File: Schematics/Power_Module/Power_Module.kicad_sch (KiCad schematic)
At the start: 50 parts, among them J1 ScrewSwitch A, J2 ScrewSwitch B, J3 Battery B, J5 Battery A, J6 Stack Male Edge Connector, Q1 AO4447A, Q2 AO4447A, U1 LMR51430XDDCR, U2 LMR51430XDDCR, U3 LMR51430XDDCR

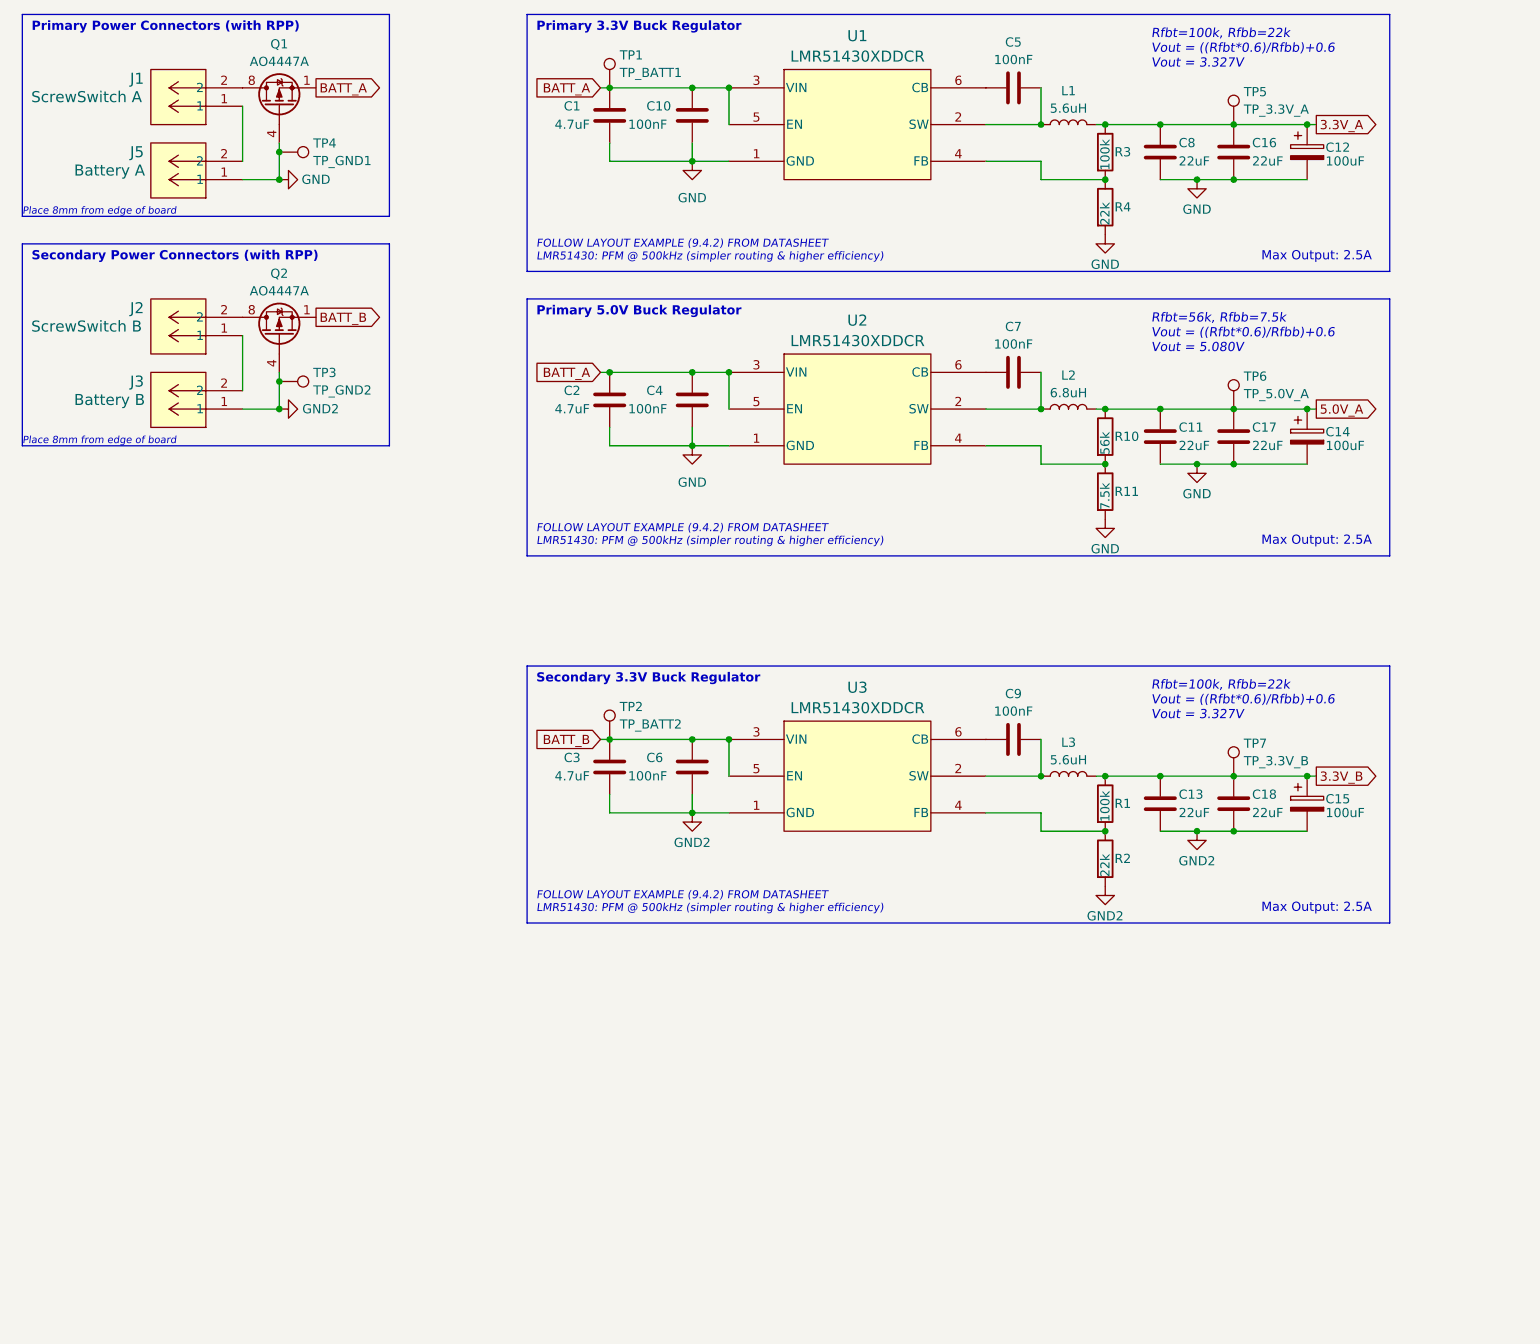
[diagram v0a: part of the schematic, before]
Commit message: Revision bump to V2.0
Changed to V2.0 due to significant hardware changes
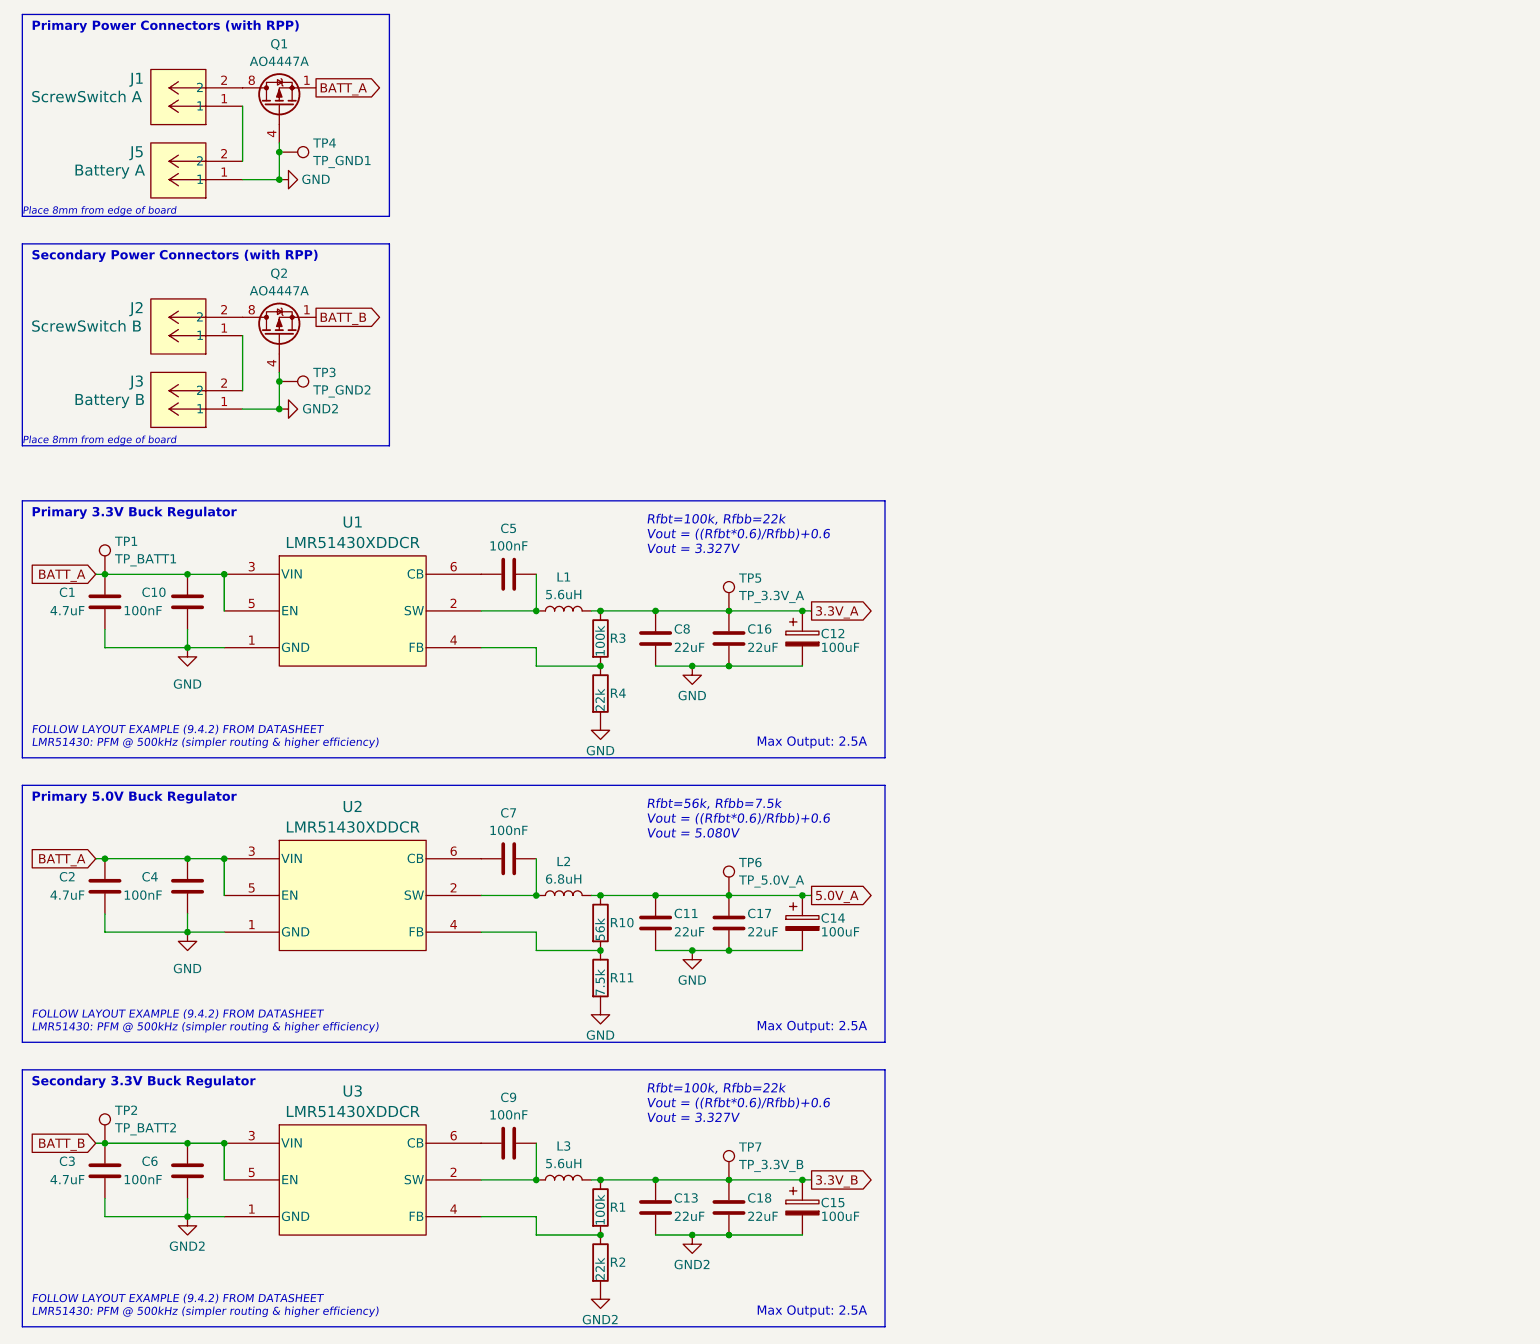
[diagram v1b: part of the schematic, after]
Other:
- title: QRET 23-24 SRAD Power Module -> QRET 23-25 SRAD Power Module
- moved on the sheet: C1, C10, C11, C12, C13, C14, C15, C16, C17, C18, C2, C3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

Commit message: Added MCUs + sensors to schematic
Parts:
- added C19, C20: 10uF, Capacitor_SMD:C_0603_1608Metric, symbol Device:C
- added C21, C22, C44, C45, C46: 0.1u, Capacitor_SMD:C_0603_1608Metric, symbol Device:C
- added C23, C24: 10p, Capacitor_SMD:C_0603_1608Metric, symbol Device:C
- added C25, C26, C27, C28, C29, C30, C31, C32: 100n, Capacitor_SMD:C_0402_1005Metric, symbol Device:C
- added C33, C36: 10n, Capacitor_SMD:C_0603_1608Metric, symbol Device:C
- added C34, C35, C37, C38: 1uF, Capacitor_SMD:C_0805_2012Metric, symbol Device:C_Polarized
- added C39, C40, C41, C42, C43: 1uF, Capacitor_SMD:C_0603_1608Metric, symbol Device:C
- added C47, C48: 100nF, Capacitor_SMD:C_0603_1608Metric, symbol Device:C
- added D4, D6: WS2812B, LED_SMD:LED_WS2812B_PLCC4_5.0x5.0mm_P3.2mm, symbol LED:WS2812B
- added D5, D8: DB_LED (YLW), LED_SMD:LED_0603_1608Metric, symbol Device:LED
- added FB1, FB2: 100R, Resistor_SMD:R_0805_2012Metric, symbol Device:FerriteBead
- added J4: USB_C_Female_USB2_Small, footprints:USB_C_DB-108PWB, symbol USB_C:USB_C_Female_USB2_Small
- added J7, J8: SWD_B, SWD_Header:SWD_PinHeader_1x04_P2.54mm_Horizontal_SMD, symbol EdgeConnector:SWD_01x04_Pin
- added R12, R15, R5: 30k, Resistor_SMD:R_0603_1608Metric, symbol Device:R
- added R13, R21, R22, R6: 10k, Resistor_SMD:R_0603_1608Metric, symbol Device:R
- added R14: 60k, Resistor_SMD:R_0603_1608Metric, symbol Device:R
- added R16: 1.5k, Resistor_SMD:R_0603_1608Metric, symbol Device:R
- added R17, R18: 5.1k, Resistor_SMD:R_0603_1608Metric, symbol Device:R
- added R19, R20: 680R, Resistor_SMD:R_0603_1608Metric, symbol Device:R
- added R23, R25, R26, R28: 100k, Resistor_SMD:R_0603_1608Metric, symbol Device:R
- added R24, R27: JMP, Resistor_SMD:R_0603_1608Metric_Pad0.98x0.95mm_HandSolder, symbol Device:R
- added TP8: TP_GND, TestPoint:TestPoint_Pad_1.5x1.5mm, symbol Connector:TestPoint
- added U10: ISO1042BDWVR, ISO1042:SOIC-8 ISO1042BDWV, symbol ISO1042BQDWVQ1:ISO1042BQDWVQ1
- added U11, U12, U13, U14, U15: LM66100DCKR, LMR66100:SC-70-6_Handsoldering, symbol QRET_Buck_PSU-symbols:LM66100DCKR
- added U4, U5: STM32F103C8Tx, Package_QFP:LQFP-48_7x7mm_P0.5mm, symbol MCU_ST_STM32F1:STM32F103C8Tx
- added U6, U7, U8: ACS37041KLHBLT-010B3, footprints:APS12628LLHALTBAP_HandSolder, symbol ACS37041KLHBLT-010B3:ACS37041KLHBLT-010B3
- added U9: AMS1117-3.3, Package_TO_SOT_SMD:SOT-223-3_TabPin2, symbol Regulator_Linear:AMS1117-3.3
- added Y1: X322516MMB4SI, Crystal:Crystal_SMD_3225-4Pin_3.2x2.5mm, symbol Device:Crystal_GND24
- R7: value 1.2k -> 3.3k; LCSC C22765 -> C22978
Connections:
- net 3.3V_A: now also C42.1, U14.1 (VIN), U6.2 (IP-); no longer C12.1, C16.1, C8.1, L1.2, R3.1, TP5.1
- net 3.3V_B: now also C39.1, U11.1 (VIN), U8.2 (IP-); no longer C13.1, C15.1, C18.1, L3.2, R1.1, TP7.1
- net 5.0V_A: now also C22.2, R14.1, U10.8 (VCC2), U7.2 (IP-); no longer C11.1, C14.1, C17.1, L2.2, R10.1, TP6.1
- net BATT_A: now also R5.1
- net BATT_B: now also R12.1
- net GND: now also C21.1, C22.1, C26.1, C27.1, C28.1, C29.1, C33.2, C34.2, C35.2, C42.2, C43.2, C44.2, C45.2, C48.2, D4.3 (VSS), D5.1 (K), D6.3 (VSS), J8.1 (GND), R15.2, R23.1, R25.1, R6.2, U10.4 (GND1), U10.5 (GND2), U14.2 (GND), U14.5 (ST), U15.2 (GND), U15.5 (ST), U4.23 (VSS), U4.35 (VSS), U4.47 (VSS), U4.8 (VSSA), U6.3 (GND), U7.3 (GND)
- net GND2: now also C19.2, C20.2, C23.2, C24.2, C25.1, C30.1, C31.1, C32.1, C36.2, C37.2, C38.2, C39.2, C40.2, C41.2, C46.2, C47.2, D8.1 (K), J4.A1 (GND), J4.A12 (GND), J4.B1 (GND), J4.B12 (GND), J7.1 (GND), R13.2, R17.2, R18.2, R26.1, R28.1, U11.2 (GND), U11.5 (ST), U12.2 (GND), U12.5 (ST), U13.2 (GND), U13.5 (ST), U5.23 (VSS), U5.35 (VSS), U5.47 (VSS), U5.8 (VSSA), U8.3 (GND), U9.1 (GND), Y1.2, Y1.4
- net CAN_L: now reaches J6.B13 (CAN_L)
- net CAN_L: now also U10.6 (CANL)
- net CAN_H: now reaches J6.B14 (CAN_H)
- net CAN_H: now also U10.7 (CANH)
- new net: C19.1, J4.A4 (VBUS), J4.A9 (VBUS), J4.B4 (VBUS), J4.B9 (VBUS), U9.3 (VI)
- new net: D4.2 (DOUT), D6.4 (DIN)
- new net: D5.2 (A), R19.1
- new net: J4.A5 (CC1), R17.1
- new net: D8.2 (A), R20.1
- new net: J4.B5 (CC2), R18.1
- new net 3.3VA_A: C33.1, C34.1, FB1.1, U4.9 (VDDA)
- new net 3.3VA_B: C36.1, C37.1, FB2.1, U5.9 (VDDA)
- new net 3.3V_A_CURR_SENSE: U4.12 (PA2), U6.4 (VOUT)
- new net 3.3V_A_Pre: C12.1, C16.1, C8.1, L1.2, R3.1, TP5.1, U6.1 (IP+)
- new net 3.3V_B_CURR_SENSE: U5.19 (PB1), U8.4 (VOUT)
- new net 3.3V_B_Pre: C13.1, C15.1, C18.1, L3.2, R1.1, TP7.1, U8.1 (IP+)
- new net 5.0V_A_CURR_SENSE: U4.13 (PA3), U7.4 (VOUT)
- new net 5.0V_A_Pre: C11.1, C14.1, C17.1, L2.2, R10.1, TP6.1, U7.1 (IP+)
- new net 5.0V_A_SENSE: R14.2, R15.1, U4.11 (PA1)
- new net BATT_A_SENSE: R5.2, R6.1, U4.10 (PA0)
- new net BATT_B_SENSE: R12.2, R13.1, U5.18 (PB0)
- new net BOOT0_A: R23.2, R24.2, U4.44 (BOOT0)
- new net BOOT0_B: R26.2, R27.2, U5.44 (BOOT0)
- new net BOOT1_A: R25.2, U4.20 (PB2)
- new net BOOT1_B: R28.2, U5.20 (PB2)
- new net CAN_RX: U10.3 (RXD), U4.45 (PB8)
- new net CAN_TX: U10.2 (TXD), U4.46 (PB9)
- new net DB_LED_A: R19.2, U4.38 (PA15)
- new net DB_LED_B: R20.2, U5.38 (PA15)
- new net OSC_IN: C23.1, U5.5 (PD0), Y1.1
- new net OSC_OUT: C24.1, U5.6 (PD1), Y1.3
- new net RGB_DATA: D4.4 (DIN), U4.39 (PB3)
- new net STM_RESET_A: C48.1, R22.1, U4.7 (NRST)
- new net STM_RESET_B: C47.1, R21.1, U5.7 (NRST)
- new net SWCLK_A: J8.4 (SWCLK), U4.37 (PA14)
- new net SWCLK_B: J7.4 (SWCLK), U5.37 (PA14)
- new net SWDIO_A: J8.3 (SWDIO), U4.34 (PA13)
- new net SWDIO_B: J7.3 (SWDIO), U5.34 (PA13)
- new net USB_D+: J4.A6 (D+), J4.B6 (D+), R16.2, U5.33 (PA12)
- new net USB_D-: J4.A7 (D-), J4.B7 (D-), U5.32 (PA11)
- new net V_MUX_A: C21.2, C26.2, C27.2, C28.2, C29.2, C35.1, C44.1, C45.1, D4.1 (VDD), D6.1 (VDD), FB1.2, R22.2, R24.1, U10.1 (VCC1), U14.3 (*CE), U14.6 (VOUT), U15.3 (*CE), U15.6 (VOUT), U4.1 (VBAT), U4.24 (VDD), U4.36 (VDD), U4.48 (VDD), U6.5 (VDD), U7.5 (VDD)
- new net V_MUX_B: C25.2, C30.2, C31.2, C32.2, C38.1, C46.1, FB2.2, R16.1, R21.2, R27.1, U11.3 (*CE), U11.6 (VOUT), U12.3 (*CE), U12.6 (VOUT), U13.3 (*CE), U13.6 (VOUT), U5.1 (VBAT), U5.24 (VDD), U5.36 (VDD), U5.48 (VDD), U8.5 (VDD)
- new net V_REGUSB_B: C20.1, C40.1, U12.1 (VIN), U9.2 (VO)
- new net V_SWD_A: C43.1, J8.2 (3V3), U15.1 (VIN)
- new net V_SWD_B: C41.1, J7.2 (3V3), U13.1 (VIN)
- no-connect marks 3 -> 58
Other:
- note added: ""main""
- note added: ""passthru""
- note added: "A"
- note added: "B"
- note added: "B0 HIGH = PROGRAMMING MODE B0 LOW = RUN MEMORY"
- note added: "CHANGE 5.0V POWER LED BRIGHTNESS (GRN ALREADY DONE)"
- note added: "CHANGE ALL "LCSC" TO "JLCPCB""
- note added: "Galvanic isolation barrier (we're not using isolation for primary modules)"
- note added: "Mount connector at edge of board"
- note added: "STM32 decoupling caps; place close to 3.3V pins"
- note added: "The WS2812B needs at least 3.5V input, but we're only using 3.3V This may cause problems"
- note added: "Vf=2.1V, I=1.8mA, R=680"
- note added: "Vin=3.3V, Vf=2.8V, R=0.15mA, R=3.3k"
- note added: "[A] Additional Filtering for Analogue VDD"
- note added: "[A] CANBUS Interface"
- note added: "[A] Ideal Diodes (MUX)"
- note added: "[A] RGB + Debug LEDs"
- note added: "[A] STM32 Boot Mode"
- note added: "[A] STM32 Decoupling Capacitors for VBAT/VDD"
- note added: "[A] Serial Wire Debug"
- note added: "[A] Voltage + Current Sensors"
- note added: "[B] Additional Filtering for Analogue VDD"
- note added: "[B] Crystal Oscillator"
- note added: "[B] Debug LED"
- note added: "[B] Ideal Diodes (MUX)"
- note added: "[B] STM32 Decoupling Capacitors for VBAT/VDD"
- note added: "[B] STM32 Reset"
- note added: "[B] Serial Wire Debug"
- note added: "[B] USB Connection"
- note added: "[B] Voltage + Current Sensors"
- moved on the sheet: C1, C10, C11, C12, C14, C16, C17, C2, C4, C5, C7, C8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

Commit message: Completed PCB layout
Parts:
- removed D4, D6: WS2812B, LED_SMD:LED_WS2812B_PLCC4_5.0x5.0mm_P3.2mm, symbol LED:WS2812B
- added C49, C50: 0.1u, Capacitor_SMD:C_0603_1608Metric_Pad1.08x0.95mm_HandSolder, symbol Device:C
- added JP1: USB_V_EN, Jumper:SolderJumper-2_P1.3mm_Open_RoundedPad1.0x1.5mm, symbol Jumper:Jumper_2_Open
- added TP10: B.S, TestPoint:TestPoint_Pad_1.5x1.5mm, symbol Connector:TestPoint
- added TP11: 3B.C.S, TestPoint:TestPoint_Pad_1.5x1.5mm, symbol Connector:TestPoint
- added TP12: 3ACS, TestPoint:TestPoint_Pad_1.5x1.5mm, symbol Connector:TestPoint
- added TP13: 5ACS, TestPoint:TestPoint_Pad_1.5x1.5mm, symbol Connector:TestPoint
- added TP16: PA7B, TestPoint:TestPoint_Pad_1.5x1.5mm, symbol Connector:TestPoint
- added TP17: PA6B, TestPoint:TestPoint_Pad_1.5x1.5mm, symbol Connector:TestPoint
- added TP9: A.S, TestPoint:TestPoint_Pad_1.5x1.5mm, symbol Connector:TestPoint
- added U16: SCM3721ASA, Package_SO:SOIC-8_3.9x4.9mm_P1.27mm, symbol SCM3721ASA:SCM3721ASA
- R24: value JMP -> BT0_A
- R27: value JMP -> BT0_B
- R9: value 1.2k -> 3.3k; LCSC C22765 -> C22978
- TP1: value TP_BATT1 -> BT_A
- TP2: value TP_BATT2 -> BT_B
- TP3: value TP_GND2 -> GND2
- TP4: value TP_GND1 -> GND1
- TP5: value TP_3.3V_A -> 3v3_A
- TP6: value TP_5.0V_A -> 5V_A
- TP7: value TP_3.3V_B -> 3v3_B
- TP8: value TP_GND -> 5VSENS
- renumbered J2 to J1, J1 to J2, J5 to J3, J3 to J5
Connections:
- net 3.3V_A: no longer R7.1
- net 3.3V_A_CURR_SENSE: now also U4.14 (PA4), TP12.1; no longer U4.12 (PA2)
- net 3.3V_B: now also U8.1 (IP+); no longer R9.1, U8.2 (IP-)
- net 3.3V_B_CURR_SENSE: now also TP11.1
- net 3.3V_B_Pre: now also U8.2 (IP-); no longer U8.1 (IP+)
- net 5.0V_A: now also U7.1 (IP+); no longer U7.2 (IP-)
- net 5.0V_A_CURR_SENSE: now also U4.15 (PA5), TP13.1; no longer U4.13 (PA3)
- net 5.0V_A_Pre: now also U7.2 (IP-); no longer U7.1 (IP+)
- net 5.0V_A_SENSE: now also TP8.1
- net BATT_A_SENSE: now also TP9.1
- net BATT_B_SENSE: now also U5.11 (PA1), TP10.1; no longer U5.18 (PB0)
- net DB_LED_A: now also U4.17 (PA7); no longer U4.38 (PA15)
- net DB_LED_B: now also U5.29 (PA8); no longer U5.38 (PA15)
- net GND: now also C49.1, U16.4 (GND1)
- net GND2: now also C50.2, U16.5 (GND2)
- net V_MUX_A: now also R7.1, C49.2, U16.1 (VDD1); no longer C44.1, C45.1, U6.5 (VDD), U7.5 (VDD)
- net V_MUX_B: now also R9.1, C50.1, JP1.1 (A), U16.8 (VDD2); no longer C46.1, U12.3 (*CE), U12.6 (VOUT), U8.5 (VDD)
- net at U5.16 (PA6): now also TP17.1
- net at U5.17 (PA7): now also TP16.1
- net TX_B: now reaches U5.30 (PA9)
- net TX_B: now also U16.7 (In_A)
- net RX_B: now reaches U5.31 (PA10)
- net RX_B: now also U16.6 (Out_B)
- net 3.3V_A_ACS_PWR: now reaches U4.16 (PA6)
- net 3.3V_A_ACS_PWR: now also C44.1, U6.5 (VDD)
- net TX_A: now reaches U4.30 (PA9)
- net TX_A: now also U16.3 (In_B)
- net RX_A: now reaches U4.31 (PA10)
- net RX_A: now also U16.2 (Out_A)
- net CAN_H renamed CAN_+
- net CAN_L renamed CAN_-
- net RGB_DATA: no longer names the net of U4.39 (PB3)
- new net: JP1.2 (B), U12.3 (*CE), U12.6 (VOUT)
- new net 3.3V_B_ACS_PWR: C46.1, U5.18 (PB0), U8.5 (VDD)
- new net 5.0V_A_ACS_PWR: C45.1, U4.12 (PA2), U7.5 (VDD)
- no-connect marks 58 -> 49
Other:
- note added: "ACS37041 draws ~12mA"
- note added: "CONSIDER ADDING NTC TEMP SENSOR?"
- note added: "DONT BE AFRAID TO MOUNT STUFF ON BOTTOM LAYER, SO LONG AS ITS MANUALLY INSTALLED"
- note added: "Place 4mm from edge of board"
- note added: "REDUCE COMPONENTS WHEREVER POSSIBLE -> CONSIDER REMOVING LM66100 & SOME AVDD FILTER CAPS"
- note added: "This module is already going to be very different from a standard module. It does not have to be as user-friendly; it already doesn't have reset/boot buttons. Maybe remove most LMR66100s and only add ones to prevent it from back-powering the entire stack."
- note added: "[A/B] Digital Isolator"
- note added: "[A] Debug LED"
- note removed: "Place 8mm from edge of board"
- note removed: "The WS2812B needs at least 3.5V input, but we're only using 3.3V This may cause problems"
- note removed: "Vin=3.3V, Vf=2.8V, I=0.4mA, R=1.2k"
- note removed: "[A] RGB + Debug LEDs"
- moved on the sheet: C19, C20, C40, C41, C44, C45, D5, R12, R13, R14, R15, R19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
